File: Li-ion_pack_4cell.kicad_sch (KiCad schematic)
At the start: 0 parts

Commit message: changes to library paths and initialized schematic
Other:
- company: (none) -> Egill Milan Gunnarsson
- title: (none) -> Li-Ion pack 4 cell
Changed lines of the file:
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@@
 	(generator_version "9.0")
 	(paper "A4")
+	(title_block
+		(title "Li-Ion pack 4 cell")
+		(date "2025-08-05")
+		(rev "1.0")
+		(company "Egill Milan Gunnarsson")
+		(comment 1 "Author")
+	)
 	(sheet_instances
 		(path "/"

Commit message: added bms, hierarchy and other stuff
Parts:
- added C1, C6: 1µ, Capacitors:C_1206_3216Metric, symbol Capacitors:C1206-1u-10%-100V-MLCC-SMD
- added C2: 4µ7, Capacitors:C_0805_2012Metric, symbol Capacitors:C0805-4u7-10%-25V-MLCC-SMD
- added C3: 100n, Capacitors:C_0805_2012Metric, symbol Capacitors:C0805-100n-10%-25V-MLCC-SMD
- added C4, C5, C7: 22µ, Capacitors:C_0805_2012Metric, symbol Capacitors:C0805-22u-20%-35V-MLCC-SMD
- added D1: LED_Yellow, Diodes:LED_1206_3216Metric, symbol Diodes:LED-1206-Yellow-1.9V-SMD
- added D2: LED_Green, Diodes:LED_1206_3216Metric, symbol Diodes:LED-1206-Green-2.4V-SMD
- added J1: J-Molex_USB_C_2.0-Female-SMD-6p, Connectors:Molex_USB-C_2.0_6p, symbol Connectors:J-Molex_USB_C_2.0-Female-SMD-6p
- added JP1: ~, Jumpers:JP-3_Bridged12-RoundedPad1.0x1.5mm-Solder, symbol Jumpers:JP-3_Bridged12-RoundedPad1.0x1.5mm-Solder
- added JP2: ~, Jumpers:JP-2_Bridged-RoundedPad1.0x1.5mm-Solder, symbol Jumpers:JP-2_Bridged-RoundedPad1.0x1.5mm-Solder
- added L1: 1µ5, Inductors:L_2020_5050Metric, symbol Inductors:L-2020-1.5µ-20%-6A-18mOhm-100kHz-SMD
- added R1, R13: 33k, Resistors:R_0805_2012Metric, symbol Resistors:R0805-33k-0.5%-0.125W-SMD
- added R14: 12k, Resistors:R_0805_2012Metric, symbol Resistors:R0805-12k-0.5%-0.125W-SMD
- added R15, R16, R2, R3: 5k1, Resistors:R_0805_2012Metric, symbol Resistors:R0805-5k1-1%-0.125W-SMD
- added R17: 390k, Resistors:R_0805_2012Metric, symbol Resistors:R0805-390k-1%-0.125W-SMD
- added R18: 22k, Resistors:R_0805_2012Metric, symbol Resistors:R0805-22k-0.5%-0.125W-SMD
- added R19: 8k25, Resistors:R_0805_2012Metric, symbol Resistors:R0805-8k25-0.5%-0.125W-SMD
- added R20: 261k, Resistors:R_0805_2012Metric, symbol Resistors:R0805-261k-1%-0.125W-SMD
- added R4, R5, R6: 10R, Resistors:R_1206_3216Metric, symbol Resistors:R1206-10R-0.1%-0.250W-SMD
- added R7, R8: 1k5, Resistors:R_0805_2012Metric, symbol Resistors:R0805-1k5-0.5%-0.125W-SMD
- added RT1: Thermistor_NTC, symbol Resistors:RT-10k-1%-0.05W-THM_free_hanging_35mm
- added TP1: CV, Mech:TP-1.0mm-THM, symbol Mech:TP-1.0mm-THM
- added TP10: VLIM, Mech:TP-1.0mm-THM, symbol Mech:TP-1.0mm-THM
- added TP11: VIN, Mech:TP-1.0mm-THM, symbol Mech:TP-1.0mm-THM
- added TP12: VCC, Mech:TP-1.0mm-THM, symbol Mech:TP-1.0mm-THM
- added TP13: VNTC, Mech:TP-1.0mm-THM, symbol Mech:TP-1.0mm-THM
- added TP14: VSYS, Mech:TP-1.0mm-THM, symbol Mech:TP-1.0mm-THM
- added TP2: SDA, Mech:TP-1.0mm-THM, symbol Mech:TP-1.0mm-THM
- added TP3: SCL, Mech:TP-1.0mm-THM, symbol Mech:TP-1.0mm-THM
- added TP6: GND, Mech:TP-1.0mm-THM, symbol Mech:TP-1.0mm-THM
- added TP7: AGND, Mech:TP-1.0mm-THM, symbol Mech:TP-1.0mm-THM
- added TP8: MID, Mech:TP-1.0mm-THM, symbol Mech:TP-1.0mm-THM
- added U1: MP2672AGD-0000, Integrated_Circuits:VFQFN-18_2x3mm_P0.4mm, symbol Integrated_Circuits:U-BATT_CHG-MP2672A-QFN-18-SMD
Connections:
- new net: D2.2 (A), R7.2
- new net: C3.2, L1.2, U1.12 (SW), U1.2 (SW)
- new net: D1.2 (A), R8.2
- new net: R17.2, R18.2, R19.1, R20.1, TP13.1, U1.8 (NTC)
- new net: R2.2, R3.1
- new net: R19.2, R20.2, RT1.1
- new net: JP1.1 (A), R1.1
- new net: C3.1, U1.3 (BST)
- new net: R2.1, U1.5 (ISET)
- new net: R5.1, R6.2
- new net: J1.A5 (CC1), R15.1
- new net: J1.B5 (CC2), R16.1
- new net: R4.1, R5.2
- new net AGND: JP2.1 (A), R1.2, R14.2, R3.2, RT1.2, TP7.1, U1.6 (AGND)
- new net BATT: C7.1, U1.10 (BATT)
- new net Battery Pack/BATTMID: R6.1
- new net CV: JP1.2 (C), TP1.1, U1.17 (CV)
- new net GND: C1.2, C2.2, C4.2, C5.2, C6.2, C7.2, J1.A12 (GND), J1.B12 (GND), JP2.2 (B), R15.2, R16.2, TP6.1, U1.13 (PGND)
- new net MID: R4.2, TP8.1, U1.9 (MID)
- new net SCL: TP3.1, U1.14 (SCL)
- new net SDA: TP2.1, U1.15 (SDA)
- new net VCC: C1.1, JP1.3 (B), R17.1, R18.1, R7.1, R8.1, TP12.1, U1.4 (VCC)
- new net VIN: C2.1, J1.A9 (VBUS), J1.B9 (VBUS), L1.1, R13.1, TP11.1, U1.1 (IN)
- new net VLIM: R13.2, R14.1, TP10.1, U1.7 (VLIM)
- new net VSYS: C4.1, C5.1, C6.1, TP14.1, U1.11 (SYS)
- new net ~{ACOK}: D2.1 (K), U1.18 (~{ACOK})
- new net ~{STAT}: D1.1 (K), U1.16 (~{STAT})
- no-connect marks 0 -> 1
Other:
- added sheet Battery Pack (BatteryPack.kicad_sch)
- added sheet Output Section (OutputSection.kicad_sch)
- note added: "R_{NTC}"
- note added: "R_{T1}"
- note added: "R_{T2}"

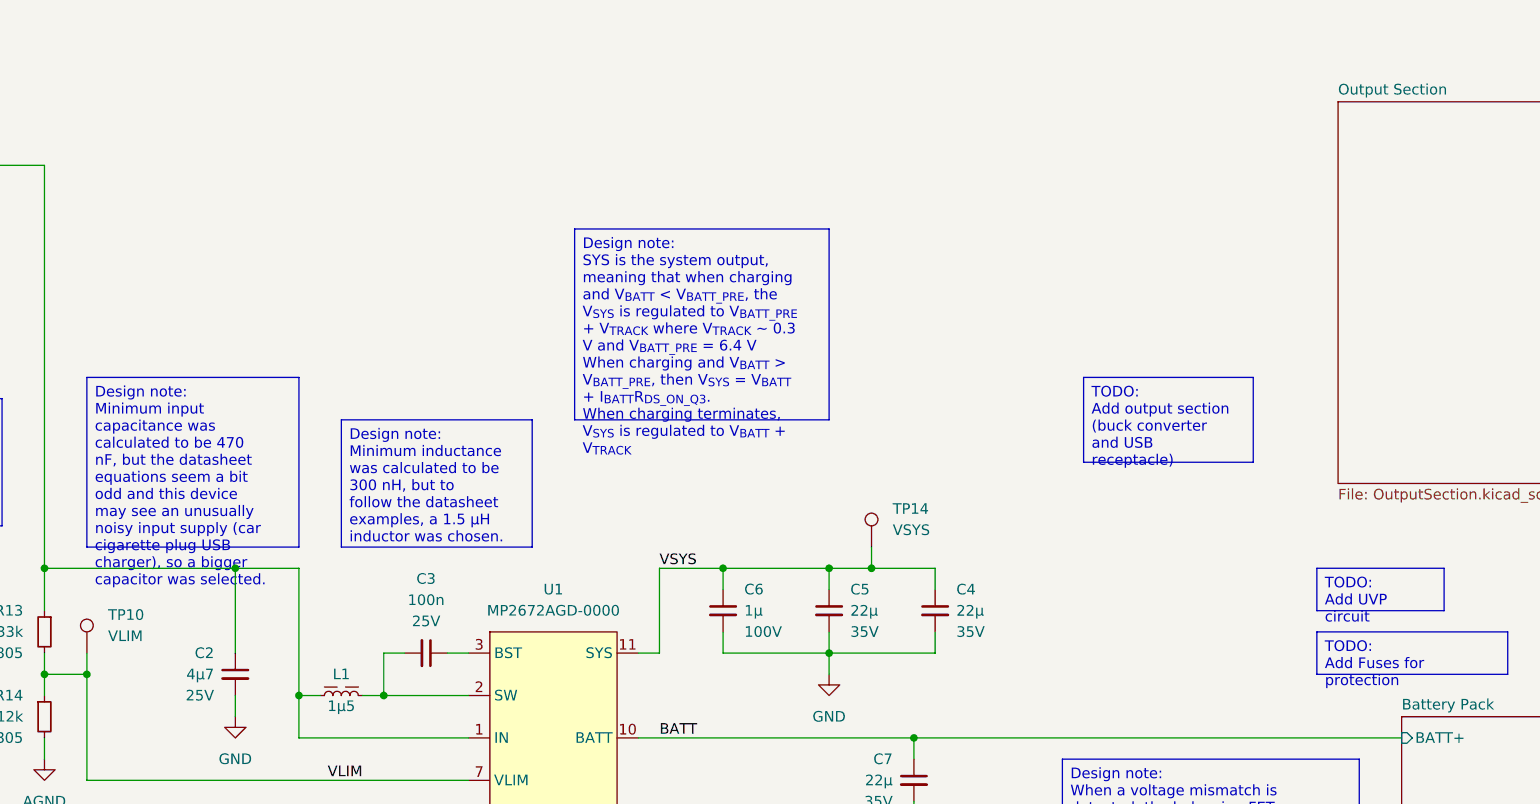
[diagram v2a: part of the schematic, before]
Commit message: parts added to schematic
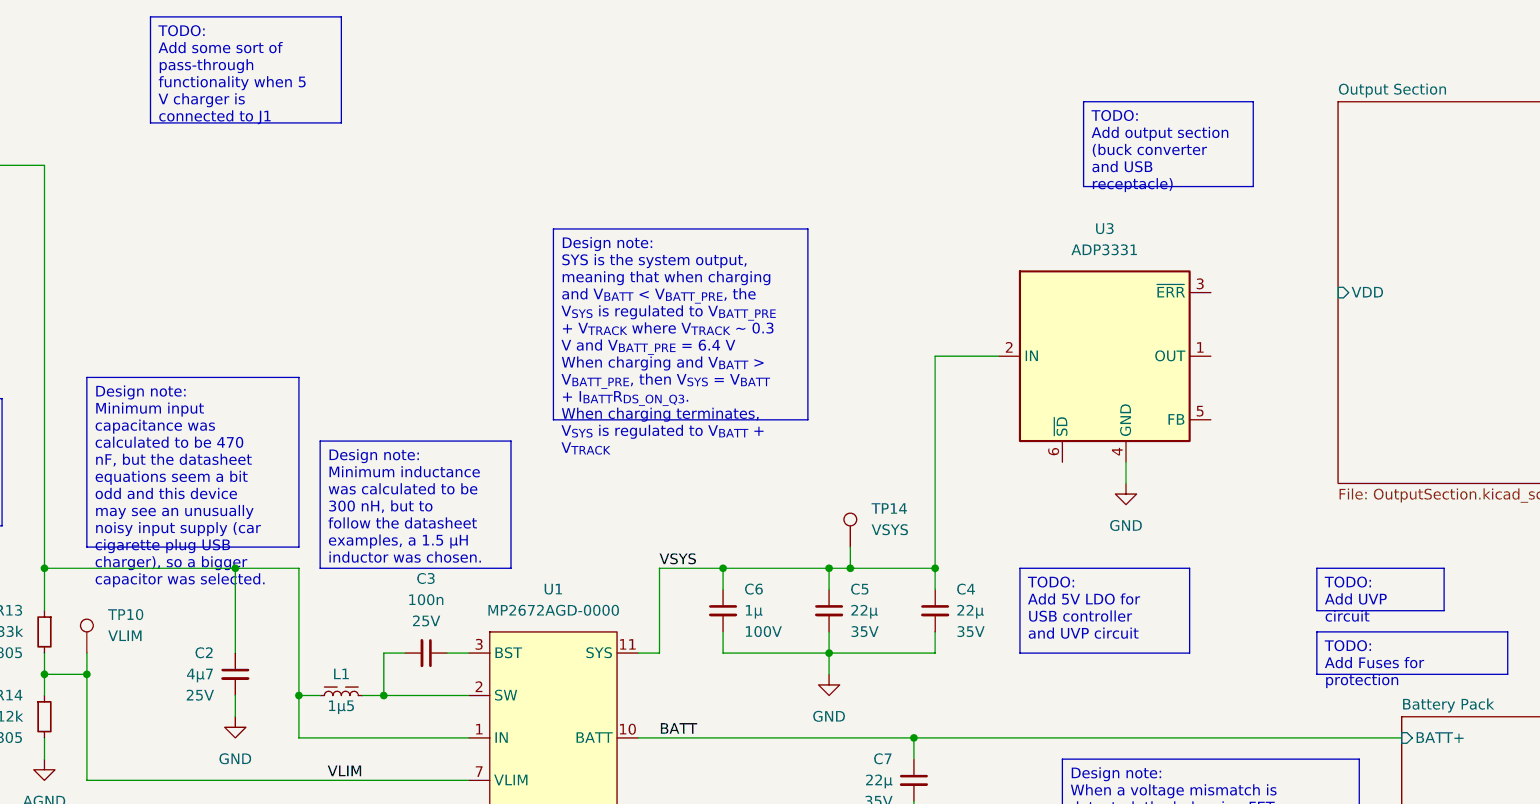
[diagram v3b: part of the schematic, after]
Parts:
- added U3: ADP3331, Integrated_Circuits:SOT-23-6, symbol Integrated_Circuits:U-LDO_regulator-ADP3331-SOT-23-6-SMD
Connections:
- net GND: now also U3.4 (GND)
- net VSYS: now also U3.2 (IN)
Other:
- sheet Output Section ports: added VDD; removed none
- moved on the sheet: TP14
